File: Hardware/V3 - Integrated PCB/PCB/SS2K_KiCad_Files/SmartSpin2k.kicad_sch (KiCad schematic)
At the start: 81 parts, among them J1 B4B-XH-AMLFSN, J2 B4B-XH-AMLFSN, J3 B8B-XH-A_LFSN, J4 10118194-0001LF, Q1 S8050, Q2 S8050, SW1 SW_Push, SW2 SW_Push, U1 ESP32-WROOM-32D, U2 TMC2209-LA-T, U3 MAX3232, U4 TPS5430DDA, U5 INTERFACE-CP2102-GMR(QFN28), U6 LM1117-3.3

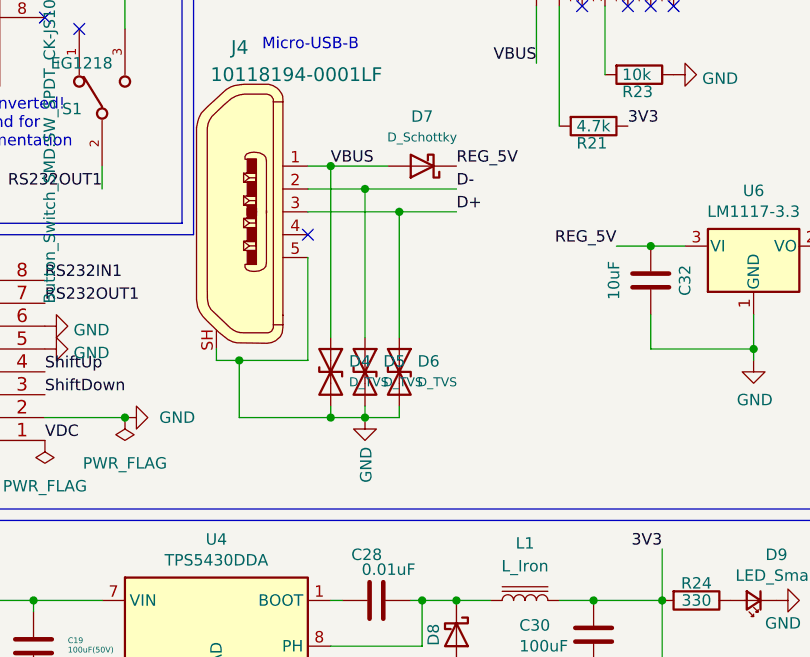
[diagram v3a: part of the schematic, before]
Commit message: Switched to TVS IC instead of individuals
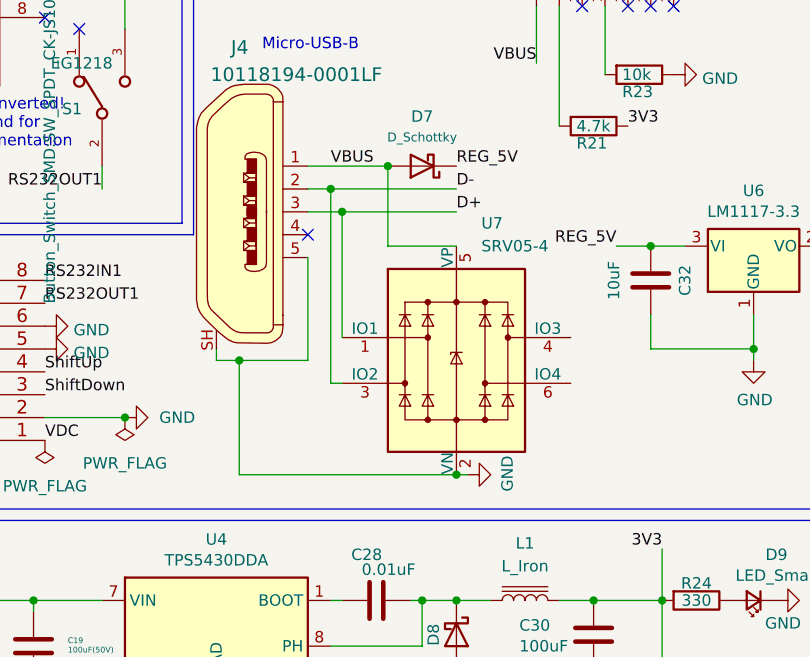
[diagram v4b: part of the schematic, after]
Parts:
- removed D4, D5, D6: D_TVS, Diode_SMD:D_0603_1608Metric, symbol Device:D_TVS
- added U7: SRV05-4, Package_TO_SOT_SMD:SOT-23-6, symbol Power_Protection:SRV05-4
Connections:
- net D+: now also U7.1 (IO1)
- net D-: now also U7.3 (IO2)
- net GND: now also U7.2 (VN)
- net VBUS: now also U7.5 (VP)
